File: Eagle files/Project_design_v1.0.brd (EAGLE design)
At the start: 57.5 x 43.2 mm, 82 parts, among them CN1 USB_CONN, CN2 BATT_IN_JST, IC1 TPS73233DBVT, IC2 TPS73233DBVT, IC3 MCP73833T-AMI/MF, IC6 TLV379IDBVT, Q1 PMV16XN, Q2 PMV16XN, Q3 PMV16XN, Q4 PMV16XN, U3 ATMEGA32U4, Y1 16MHz

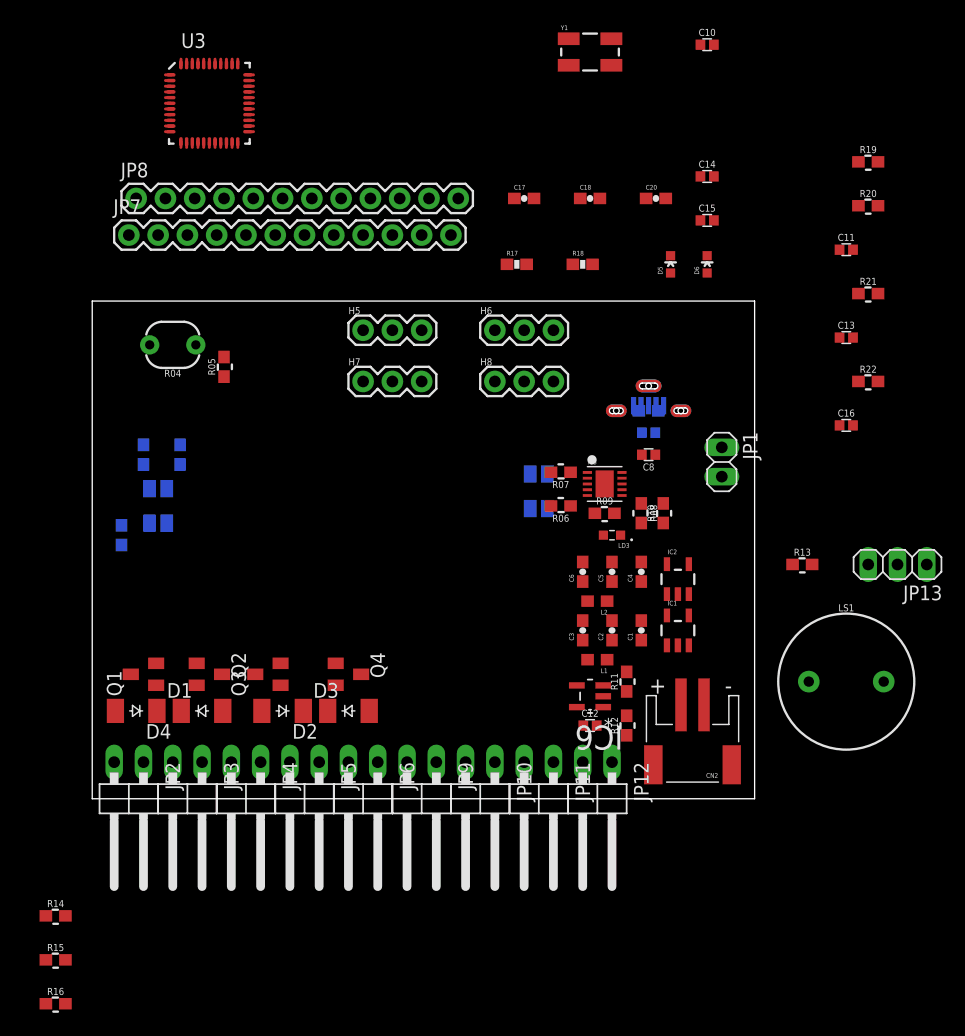
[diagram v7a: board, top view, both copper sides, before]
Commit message: PCB line + silkscreen updated
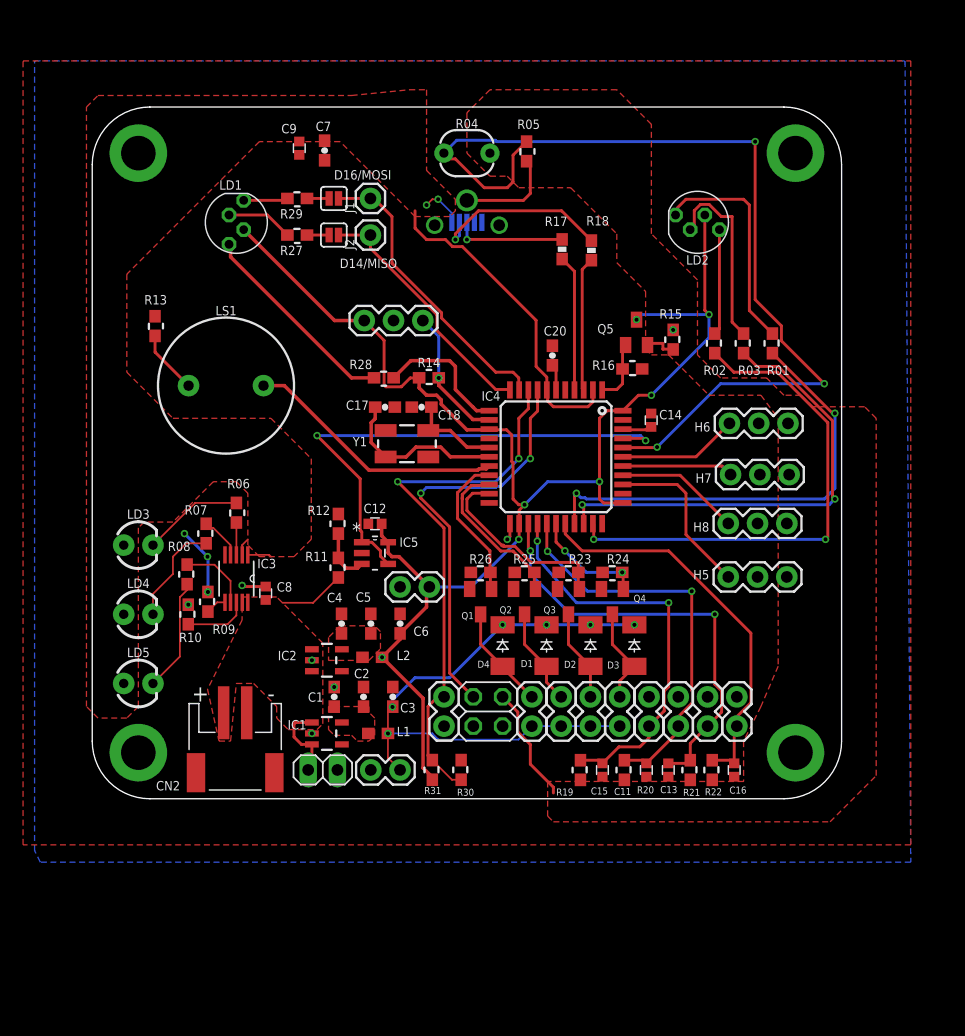
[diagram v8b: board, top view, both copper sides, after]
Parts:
- removed C10: 100n, custom_part:0402
- removed D5: Green, SparkFun:LED-0603
- removed D6: Yellow, SparkFun:LED-0603
- removed IC6: TLV379IDBVT, AD8009JRTZ-REEL:SOT95P280X145-5N
- removed JP7, JP8: (no value), SparkFun:1X12
- removed U3: ATMEGA32U4, Testing:QFN-44-NOPAD_1:1-OUTFAKES
- added D14/MISO, D16/MOSI: JUMPER-SMT_2_NO_SILK, SparkFun-Jumpers:SMT-JUMPER_2_NO_SILK
- added IC4: ATMEGA32U4, ATMEGA32U4:TQFP44
- added IC5: TLV379IDBVT, AD8009JRTZ-REEL:SOT95P280X145-5N
- added J1, J2: (no value), SparkFun-Connectors:1X01
- added J3: 455-1750-1-ND, SparkFun-Connectors:1X03
- added JP14, JP15: Connectors, SparkFun-Connectors:1X02
- added LD4: GRN, SparkFun-LED:LED_3MM
- added LD5: RED, SparkFun-LED:LED_3MM
- added Q5: PMV16XN, custom_part_2:SOT23
- added R23, R24, R25, R26, R30, R31: 10k, custom_part:0603
- added R27, R28, R29: 2k, custom_part:0603
- CN1: value USB_CONN -> WM9734TR-ND; device 105133-0011:MOLEX_105133-0011 -> SparkFun-Connectors:USB-B-MICRO-SMD_VERT
- H5: value SOIL_MOISTURE -> POT1
- H6: value SOIL_MOISTURE -> POT2
- H7: value SOIL_MOISTURE -> POT3
- H8: value SOIL_MOISTURE -> POT4
- IC3: value MCP73833T-AMI/MF -> MCP73833T-BZI/UN; device microbuilder:DFN10_3X3MM -> MCP73833T-BZI_UN:SOP50P490X110-10N
- JP10, JP11, JP12, JP2, JP3, JP4, JP5, JP6, JP9: device pinhead:1X02/90 -> SparkFun-Connectors:1X02
- JP13: device pinhead:1X03 -> pinhead:2X02
- LD1, LD2: value RGB_LED -> DIFFUSE; device Semicond:PLCC-4 -> RGB_LED:LED-RGB_THRU_5MM
- LD3: value RLED -> OR; device LTST-C190KRKT:LEDM1608X80 -> SparkFun-LED:LED_3MM
- R06, R07, R08: value 330 -> 1k
- R15, R16: value 330 -> 10k
- Y1: value 16MHz -> 8MHz
- moved R15 75.9 mm to (50.4, 39.8), turned to 270 degrees
- moved R16 74.4 mm to (46.9, 37.3), turned to 180 degrees
- moved R13 59.8 mm to (5.45, 41.0), turned to 90 degrees
- moved LS1 59.6 mm to (11.6, 35.8)
- moved R19 58.4 mm to (42.4, 2.49), turned to 270 degrees
- moved R14 56.8 mm to (29.2, 36.5), turned to 180 degrees
- moved R01 55.4 mm to (59.0, 39.5), flipped to the top, turned to 270 degrees
- moved R02 54.1 mm to (54.0, 39.5), flipped to the top
- moved R20 53.3 mm to (46.2, 2.49), turned to 270 degrees
- moved R03 49.8 mm to (56.5, 39.5), flipped to the top, turned to 270 degrees
- moved C15 48.5 mm to (44.3, 2.49), turned to 270 degrees
- moved C11 48.4 mm to (48.1, 2.49), turned to 270 degrees
- moved R21 44.1 mm to (51.9, 2.49), turned to 270 degrees
- moved JP1 43.7 mm to (20.0, 2.50), turned to 180 degrees
- moved R10 42.1 mm to (8.33, 16.0), turned to 270 degrees
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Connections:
- removed net ALARM: JP13.3
- removed net BUZZ: LS1.+
- removed net CTRL_MOTOR1: Q1.1
- removed net CTRL_MOTOR2: Q2.1
- removed net CTRL_MOTOR3: Q3.1
- removed net CTRL_MOTOR4: Q4.1
- removed net CTRL_PHOTOCELL: R04.2
- removed net D10: JP7.12, U3.30
- removed net D11: U3.12
- removed net D12: U3.26
- removed net D13: U3.32
- removed net D14: U3.8
- removed net D3: JP8.7, U3.18
- removed net D4: JP8.6, U3.25
- removed net D5: JP8.5, U3.31
- removed net D6: JP8.4, U3.27
- removed net D9: JP8.1, U3.29
- removed net LED_B: R03.2
- removed net LED_G: R01.2
- removed net LED_R: R02.2
- removed net LEVEL_SENSOR: JP12.1
- removed net MISO: JP7.10, U3.11
- removed net MOISTURE1: C15.1, JP6.1, R19.1
- removed net MOISTURE2: C11.1, JP9.1, R20.1
- removed net MOISTURE3: C13.1, JP11.1, R21.1
- removed net MOISTURE4: C16.1, JP10.1, R22.1
- removed net MOSI: JP7.11, U3.10
- removed net N$23: D6.C
- removed net N$24: D5.C
- removed net PHOTOCELL_READ: R04.1, R05.2
- removed net RXI: JP8.11, U3.20
- removed net SCK: JP7.9, U3.9
- removed net TXLED: U3.22
- removed net TXO: JP8.12, U3.21
- removed net V_BAT_SENSE: IC6.1, IC6.4
- removed net WATER_ADJ_1: H5.3
- removed net WATER_ADJ_2: H6.3
- removed net WATER_ADJ_3: H7.3
- removed net WATER_ADJ_4: H8.3
- new net A10: C15.1, IC4.26, JP6.1, R19.1
- new net A6: C13.1, IC4.25, JP11.1, R21.1
- new net A7: C11.1, IC4.27, JP9.1, R20.1
- new net A8: C16.1, IC4.29, JP10.1, R22.1
- new net CTRL_3.3V: H5.1, H6.1, H7.1, H8.1, JP13.3, Q5.2, R04.2, R15.2, R19.2, R20.2, R21.2, R22.2
- new net D10#: IC4.30, R01.2
- new net D11#: IC4.12, R28.2
- new net D13#: IC4.32, R02.2
- new net D14/MISO: D14/MISO.2, IC4.11, J2.1
- new net D15/SCK: IC4.9, JP12.1, R30.2, R31.1
- new net D16/MOSI: D16/MOSI.2, IC4.10, J1.1
- new net D17/SS: IC4.8, JP13.4
- new net D3#: IC4.18, LS1.+
- new net D5#: IC4.31, R03.2
- new net N$26: LD1.1, R29.1
- new net N$28: LD1.4, R28.1
- new net N$29: LD1.2, R27.1
- new net N$30: D16/MOSI.1, R29.2
- new net N$32: D14/MISO.1, R27.2
- new net RXI/D0: IC4.20, Q2.1, R25.2
- new net TXO/D1: IC4.21, Q3.1, R23.2
- net 3.3V: now also IC4.14, IC4.24, IC4.34, IC4.44, IC5.5, J3.3, JP15.1, LD1.3, LD2.3, Q5.3, R31.2; no longer C10.1, H5.1, H6.1, H7.1, H8.1, IC6.5, JP13.1, LD1.1, R19.2, R20.2, R21.2, R22.2, U3.14, U3.24, U3.34, U3.44
- net 5.0V: now also CN1.VBUS, IC3.1, IC3.2, IC4.2, IC4.7, LD4.A, LD5.A; no longer CN1.1, IC3.P$1, IC3.P$2, LD2.1, U3.2, U3.7
- net A0: now also H5.3, IC4.36; no longer JP7.8, U3.36
- net A1: now also H8.3, IC4.37; no longer JP7.7, U3.37
- net A2: now also H7.3, IC4.38; no longer JP7.6, U3.38
- net A3: now also H6.3, IC4.39; no longer JP7.5, U3.39
- net A4: now also IC4.40, R04.1, R05.2; no longer U3.40
- net A5: now also IC4.41, IC5.1, IC5.4; no longer U3.41
- net AREF: now also C14.1, IC4.42; no longer U3.42
- net D+: now also IC4.4; no longer U3.4
- net D-: now also IC4.3; no longer U3.3
- net D2: now also IC4.19, Q1.1, R26.2; no longer JP8.8, U3.19
- net D7: now also IC4.1, Q5.1, R16.2; no longer JP8.3, U3.1
- net D8: now also IC4.28, Q4.1, R24.2; no longer JP8.2, U3.28
- net GND: now also C14.2, CN1.GND, CN1.P1, CN1.P2, CN1.P3, IC3.5, IC4.15, IC4.23, IC4.33, IC4.35, IC4.43, IC4.5, IC5.2, J3.2, JP13.1, JP14.2, JP15.2, R15.1, R16.1, R23.1, R24.1, R25.1, R26.1, R30.1; no longer C10.2, CN1.5, CN1.6, CN1.7, CN1.8, IC3.P$5, IC6.2, JP7.1, JP7.2, JP8.10, JP8.9, U3.15, U3.23, U3.33, U3.35, U3.43, U3.5
- net N$1: now also LD2.2; no longer LD1.2
- net N$12: now also LD5.K; no longer LD3.C
- net N$16: now also IC3.6; no longer IC3.P$6
- net N$17: now also IC5.3; no longer IC6.3
- net N$18: now also IC4.17; no longer U3.17
- net N$19: now also IC4.6; no longer U3.6
- net N$20: now also CN1.D-; no longer CN1.2
- net N$21: now also CN1.D+; no longer CN1.3
- net N$3: now also LD3.K; no longer LD2.3
- net N$34: now also LD2.1; no longer LD1.3
- net N$35: now also LD2.4; no longer LD1.4
- net N$4: now also LD4.K; no longer LD2.4
- net N$5: now also IC3.4; no longer IC3.P$3
- net N$6: now also IC3.3; no longer IC3.P$4
- net N$7: now also IC3.7; no longer IC3.P$7
- net N$8: now also IC3.8; no longer IC3.P$8
- net N$9: now also IC4.16; no longer U3.16
- net RESET: now also IC4.13, J3.1; no longer JP7.3, U3.13
- net VCC: now also JP14.1; no longer D5.A, D6.A, JP7.4
- net V_BAT: now also IC3.10, IC3.9; no longer IC3.P$10, IC3.P$9
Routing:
- net 3.3V: track 0.00 -> 127.7 mm, vias 0 -> 7
- net A4: track 0.00 -> 82.2 mm, vias 0 -> 3
- net VCC: track 0.00 -> 51.3 mm, vias 0 -> 6
- net D15/SCK: track 0.00 -> 47.7 mm, vias 0 -> 2
- net A5: track 0.00 -> 44.9 mm, vias 0 -> 2
- net D13#: track 0.00 -> 44.0 mm, vias 0 -> 2
- net D5#: track 0.00 -> 40.8 mm, vias 0 -> 2
- net D10#: track 0.00 -> 39.8 mm, vias 0 -> 2
- net A6: track 0.00 -> 37.9 mm, vias 0 -> 2
- net D17/SS: track 0.00 -> 36.5 mm, vias 0 -> 2
- net A10: track 0.00 -> 35.5 mm, vias 0 -> 2
- net 5.0V: track 0.00 -> 35.4 mm, vias 0 -> 2
- net A8: track 0.00 -> 35.2 mm
- net A7: track 0.00 -> 35.0 mm, vias 0 -> 2
- net D16/MOSI: track 0.00 -> 25.8 mm
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- added copper zone on layer 1, net 5.0V
- added copper zone on layer 1, net CTRL_3.3V
- added copper zone on layer 1, net GND
- added copper zone on layer 16, net GND
- added copper zone on layer 1, net N$13
- added copper zone on layer 1, net N$2
- added copper zone on layer 1, net V_BAT
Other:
- board size 57.5 x 43.2 mm -> 65 x 60 mm
- board text added: "!RESET"
- board text added: "3.3V"
- board text added: "A0"
- board text added: "A1"
- board text added: "A10"
- board text added: "A2"
- board text added: "A3"
- board text added: "A6"
- board text added: "A7"
- board text added: "A8"
- board text added: "CHARGING"
- board text added: "C_3.3V"
- board text added: "D15/CLK"
- board text added: "D17/SS"
- board text added: "DONE"
- board text added: "GND"
- board text added: "LED RGB 5mm diam LED R/G/O 3mm diam"
- board text added: "M1"
- board text added: "M2"
- board text added: "M3"
- board text added: "M4"
- board text added: "PWR"
- board text added: "VCC"
- board text added: "V_BAT"
